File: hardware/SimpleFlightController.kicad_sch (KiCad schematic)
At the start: 0 parts

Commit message: Battery Charger 80% Done
I ended up finishing wiring all the pins except for the battery related ones, I'll finish those tomorrow and I'll move on to the sensors.
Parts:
- added C2: 44uF, symbol Device:C
- added C3, C4, C6: 10uF, symbol Device:C
- added C5: 1uf, symbol Device:C
- added C7: 47uF, symbol Device:C
- added CARD1: DM3C-SF, easyeda2kicad:TF-SMD_DM3CS-SF, symbol LSCS_Parts:DM3C-SF
- added D1: LED, symbol Device:LED
- added J1: Screw_Terminal_01x02, symbol Connector:Screw_Terminal_01x02
- added L1: 1μH, symbol Device:L
- added R1, R2: 5.1K, symbol Device:R
- added R10: 5.23k, symbol Device:R
- added R11: 383, symbol Device:R
- added R14, R4, R5, R6: 10k, symbol Device:R
- added R3: 2.2k, symbol Device:R
- added R8: 10K, symbol Device:R
- added R9: 30.1k, symbol Device:R
- added U1: TPS63070RNMR, easyeda2kicad:VQFN-15_L3.0-W2.5-P0.50-BL, symbol LSCS_Parts:TPS63070RNMR
- added U2: ABX00027, easyeda2kicad:COMM-SMD_ABX00027, symbol LSCS_Parts:ABX00027
- added U3: ICM-20948, easyeda2kicad:QFN-24_L3.0-W3.0-P0.40-BL-EP, symbol LSCS_Parts:ICM-20948
- added U4: BME280, easyeda2kicad:LGA-8_BME280_BL, symbol LSCS_Parts:BME280
- added U5: BQ25887RGET, easyeda2kicad:VQFN-24_L4.0-W4.0-P0.50-TL-EP2.7, symbol LSCS_Parts:BQ25887RGET
- added U6: LMR51430XDDCR, easyeda2kicad:SOT-23-6_L2.9-W1.6-P0.95-LS2.8-BL, symbol LSCS_Parts:LMR51430XDDCR
- added USB1: TYPE-C 16PIN 2MD, easyeda2kicad:USB-C-SMD_TYPE-C-16PIN-2MD-073, symbol LSCS_Parts:TYPE-C16PIN2MD
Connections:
- new net: D1.1 (K), U5.2 (STAT)
- new net: D1.2 (A), R3.2
- new net: R2.1, USB1.B5 (CC2)
- new net: C4.1, C6.2, L1.1, U5.21 (PMID), U5.22 (PMID)
- new net: C2.1, U5.15 (SNS), U5.16 (SNS)
- new net: C7.1, U5.12 (BTST)
- new net: R14.1, U5.7 (TS)
- new net: R11.1, U5.8 (ILIM)
- new net: R10.1, R9.2
- new net: R1.1, USB1.A5 (CC1)
- new net +3.3V: R3.1, R4.1, R5.1, R6.1, R8.2
- new net +3V3: R10.2
- new net +BAT: C3.1, J1.1 (Pin_1), U5.13 (BAT), U5.14 (BAT)
- new net BQ_CD: U5.3 (CD)
- new net BQ_INT: R6.2, U5.6 (~{INT})
- new net BQ_PG: R8.1, U5.1 (~{PG})
- new net BQ_PSEL: U5.24 (PSEL)
- new net BTST: C7.2, L1.2, U5.17 (SW), U5.18 (SW)
- new net GND: C2.2, C3.2, C4.2, C5.2, C6.1, J1.2 (Pin_2), R1.2, R11.2, R14.2, R2.2, R9.1, U5.11 (REGN), U5.19 (GND), U5.20 (GND), U5.25 (EP), USB1.13 (EH), USB1.14 (EH), USB1.A1B12 (GND), USB1.B1A12 (GND)
- new net I2C_SCL: R5.2, U5.5 (SCL)
- new net I2C_SDA: R4.2, U5.4 (SDA)
- new net USB_DN: USB1.A7 (Dn1), USB1.B7 (Dn2)
- new net USB_DP: USB1.A6 (Dp1), USB1.B6 (Dp2)
- new net VBUS: C5.1, U5.23 (VBUS), USB1.A4B9 (VBUS), USB1.B4A9 (VBUS)
- no-connect marks 0 -> 2

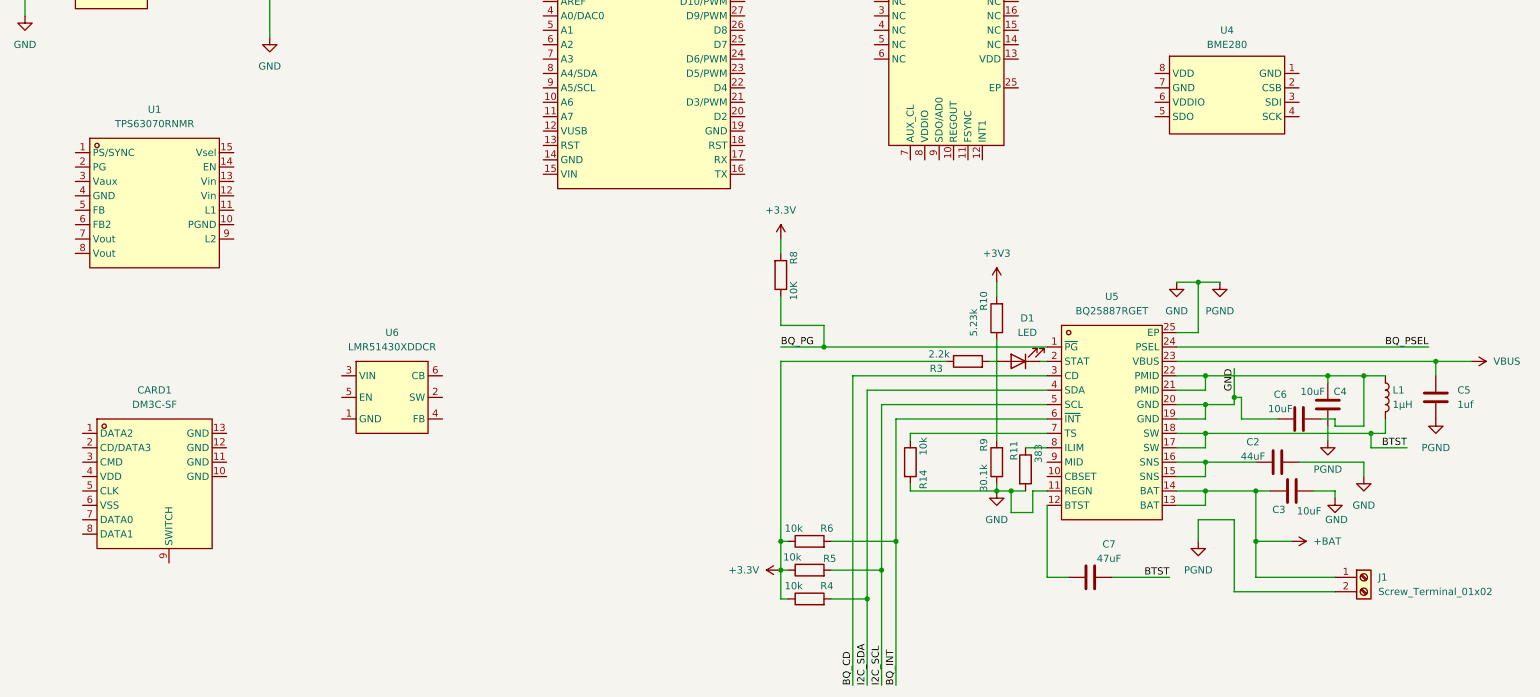
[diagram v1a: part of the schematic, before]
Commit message: 5/22/2026: Finished Regulator, Sensor, and Tracker
Everything went smoothly, using the datasheets for so long has given me a better understanding on what each symbol means/does.
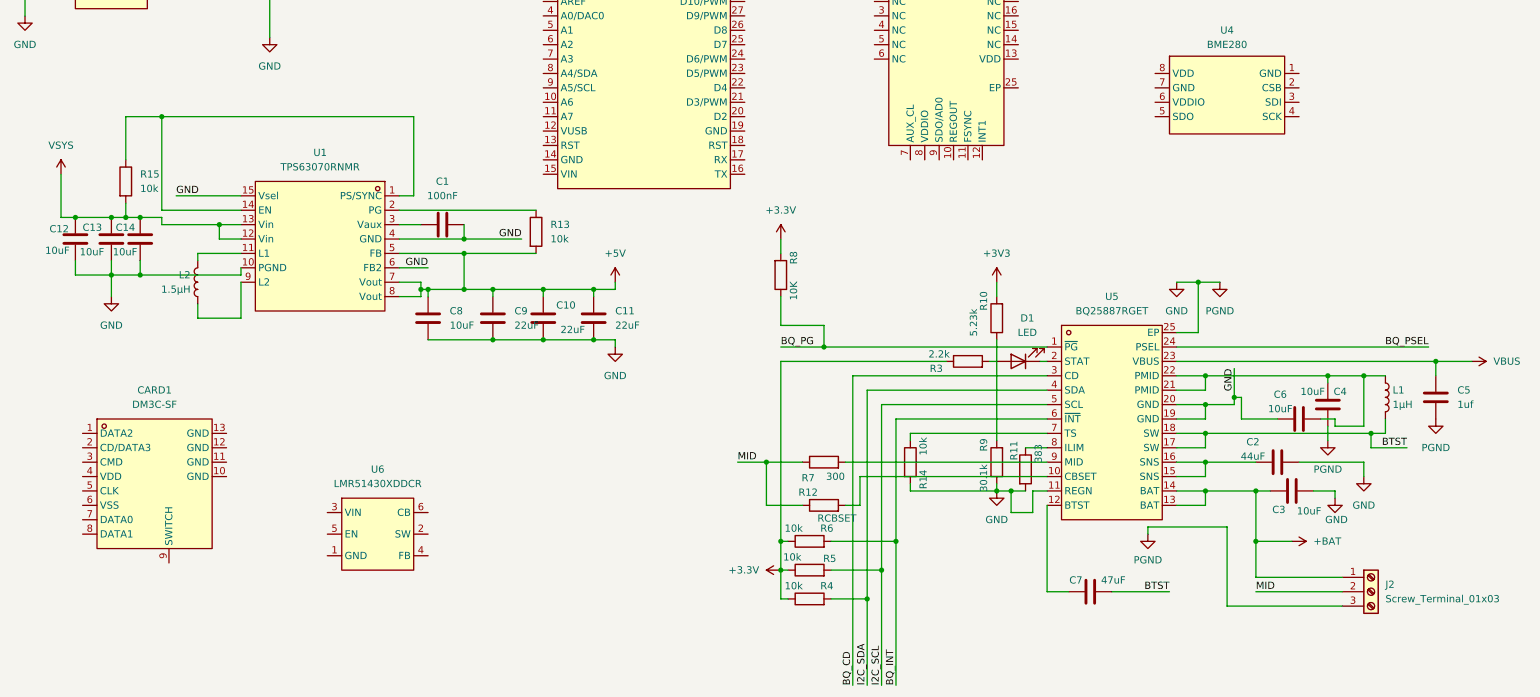
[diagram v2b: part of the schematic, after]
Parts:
- removed J1: Screw_Terminal_01x02, symbol Connector:Screw_Terminal_01x02
- added C1: 100nF, symbol Device:C
- added C10, C11, C9: 22uF, symbol Device:C
- added C12, C13, C14, C8: 10uF, symbol Device:C
- added J2: Screw_Terminal_01x03, symbol Connector:Screw_Terminal_01x03
- added L2: 1.5μH, symbol Device:L
- added R12: RCBSET, symbol Device:R
- added R13, R15: 10k, symbol Device:R
- added R7: 300, symbol Device:R
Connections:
- net +BAT: now also J2.1 (Pin_1)
- net GND: now also U1.10 (PGND), U1.15 (Vsel), U1.4 (GND), U1.6 (FB2), C1.1, C10.2, C11.2, C12.2, C13.2, C14.2, C8.2, C9.2, J2.3 (Pin_3)
- net at U5.10 (CBSET): now also R12.2
- net at U5.9 (MID): now also R7.2
- net at U1.1 (PS/SYNC): now also U1.14 (EN), R15.1
- net at U1.11 (L1): now also L2.1
- net VSYS: now reaches U1.12 (Vin)
- net VSYS: now also U1.13 (Vin), C12.1, C13.1, C14.1, R15.2
- net at U1.2 (PG): now also R13.1
- net at U1.3 (Vaux): now also C1.2
- net +5V: now reaches U1.5 (FB)
- net +5V: now also U1.7 (Vout), U1.8 (Vout), C10.1, C11.1, C8.1, C9.1, R13.2
- net at U1.9 (L2): now also L2.2
- new net MID: J2.2 (Pin_2), R12.1, R7.1
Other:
- moved on the sheet: C7, U1, U6

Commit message: Finished Schematic
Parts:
- removed U2: ABX00027, easyeda2kicad:COMM-SMD_ABX00027, symbol LSCS_Parts:ABX00027
- added C15: 2.2μF, symbol Device:C
- added C16, C17: 22μF, symbol Device:C
- added C18, C19, C20, C26, C27, C28, C29, C30, C39: 100nF, symbol Device:C
- added C21: C, symbol Device:C
- added C22, C24: 100uF, symbol Device:C
- added C25: 2.2uF, symbol Device:C
- added C31, C32, C33, C34: 1uF, symbol Device:C
- added C35, C36: 6.8pF, symbol Device:C
- added C37, C38: 20pF, symbol Device:C
- added J1, J3: Conn_01x03, symbol Connector_Generic:Conn_01x03
- added L3: 5.6μH, symbol Device:L
- added L4: FCM1608KF-601T03, easyeda2kicad:L0603, symbol LSCS_Parts:FCM1608KF-601T03
- added R16: 22.1k, symbol Device:R
- added R17: 100k, symbol Device:R
- added R18, R19, R20, R21, R22, R23, R24: 10k, symbol Device:R
- added SW1, SW2: TS-1088-AR02016, easyeda2kicad:SW-SMD_L3.9-W3.0-P4.45, symbol LSCS_Parts:TS-1088-AR02016
- added U7: STM32F722RETx, Package_QFP:LQFP-64_10x10mm_P0.5mm, symbol MCU_ST_STM32F7:STM32F722RETx
- added X1: X322525MOB4SI, easyeda2kicad:CRYSTAL-SMD_4P-L3.2-W2.5-BL, symbol LSCS_Parts:X322525MOB4SI
- added X2: Q13FC1350000400, easyeda2kicad:FC-135R_L3.2-W1.5, symbol LSCS_Parts:Q13FC1350000400
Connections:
- net +3.3V: now also CARD1.4 (VDD), U3.13 (VDD), U3.8 (VDDIO), U4.2 (CSB), U4.6 (VDDIO), U4.8 (VDD), C16.1, C17.1, C19.1, C20.1, C21.2, C24.1, C26.1, C27.1, C28.1, C29.1, C30.1, C31.1, C32.1, C33.1, C34.1, L3.2, L4.1, R18.1, R19.1, R20.1, R21.1, R22.1, R23.1, SW2.1, U7.1 (VBAT), U7.19 (VDD), U7.32 (VDD), U7.48 (VDD), U7.64 (VDD)
- net +5V: now also J1.1 (Pin_1), J3.1 (Pin_1)
- net BQ_INT: now also U7.57 (PB5)
- net GND: now also CARD1.10 (GND), CARD1.11 (GND), CARD1.12 (GND), CARD1.13 (GND), CARD1.6 (VSS), U3.18 (GND), U4.1 (GND), U4.5 (SDO), U4.7 (GND), U6.1 (GND), C15.2, C16.2, C17.2, C19.2, C20.2, C21.1, C22.2, C24.2, C25.2, C26.2, C27.2, C28.2, C29.2, C30.2, C31.2, C32.2, C33.2, C34.2, C35.2, C36.2, C37.2, C38.2, C39.1, J1.3 (Pin_3), J3.3 (Pin_3), R16.2, R24.2, SW1.1, U7.12 (VSSA), U7.18 (VSS), U7.31 (VSS), U7.47 (VSS), U7.63 (VSS), X1.2 (GND), X1.4 (GND)
- net I2C_SCL: now also U4.4 (SCK), U7.58 (PB6)
- net I2C_SDA: now also U4.3 (SDI), U7.59 (PB7)
- net USB_DN: now also U7.44 (PA11)
- net USB_DP: now also U7.45 (PA12)
- net VSYS: now also U6.3 (VIN), U6.5 (EN), C15.1
- net at D1.2 (A), R3.2: now also R10.1
- net SD_DAT2: now reaches CARD1.1 (DATA2)
- net SD_DAT2: now also R23.2, U7.51 (PC10)
- net SD_DAT3: now reaches CARD1.2 (CD/DATA3)
- net SD_DAT3: now also R22.2, U7.52 (PC11)
- net SD_CMD: now reaches CARD1.3 (CMD)
- net SD_CMD: now also R21.2, U7.54 (PD2)
- net SD_CLK: now reaches CARD1.5 (CLK)
- net SD_CLK: now also R20.2, U7.53 (PC12)
- net SD_DAT0: now reaches CARD1.7 (DATA0)
- net SD_DAT0: now also R19.2, U7.39 (PC8)
- net SD_DAT1: now reaches CARD1.8 (DATA1)
- net SD_DAT1: now also R18.2, U7.40 (PC9)
- net at U6.2 (SW): now also C18.2, L3.1, R17.1
- net at U6.4 (FB): now also R16.1, R17.2
- net at U6.6 (CB): now also C18.1
- net at U3.10 (REGOUT): now also C22.1
- net ICM_FSYNC: now reaches U3.11 (FSYNC)
- net ICM_INT1: now reaches U3.12 (INT1)
- net ICM_INT1: now also U7.24 (PC4), U7.41 (PA8)
- net ICM_nCS: now reaches U3.22 (nCS)
- net ICM_SCL: now reaches U3.23 (SCL/SCLK)
- net ICM_SDI: now reaches U3.24 (SDA/SDI)
- net ICM_SDI: now also U7.23 (PA7)
- net ICM_SDO: now reaches U3.9 (SDO/AD0)
- net ICM_SDO: now also U7.22 (PA6)
- net at R9.2: no longer R10.1
- new net: L4.2, U7.13 (VDDA)
- new net: C25.1, U7.30 (VCAP_1)
- new net BMP_INT: U7.62 (PB9)
- new net BOOT: R24.1, SW2.2, U7.60 (BOOT0)
- new net BQ_CE: U7.61 (PB8)
- new net HSE_IN: C38.1, U7.5 (PH0), X1.1 (OSC1)
- new net HSE_OUT: C37.1, U7.6 (PH1), X1.3 (OSC2)
- new net ICM_CS: U7.20 (PA4)
- new net ICM_INT2: U7.25 (PB0), U7.42 (PA9)
- new net ICM_SCK: U7.21 (PA5)
- new net LSE_IN: C36.1, U7.3 (PC14), X2.1
- new net LSE_OUT: C35.1, U7.4 (PC15), X2.2
- new net RESET: C39.2, SW1.2, U7.7 (NRST)
- new net SD_CD: U7.55 (PB3)
- new net SERVO1: J1.2 (Pin_2), U7.14 (PA0)
- new net SERVO2: J3.2 (Pin_2), U7.15 (PA1)
- no-connect marks 2 -> 39
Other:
- title: (none) -> Simple Flight Controller
- moved on the sheet: C1, C10, C11, C12, C13, C14, C2, C3, C4, C5, C6, C7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

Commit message: PCB Footprints
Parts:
- C1, C12, C13, C14, C15, C18, C19, C20, C22, C24, C25, C26, C27, C28, C29, C3, C30, C31, C32, C33, C34, C35, C36, C37, C38, C39, C4, C5, C6, C8: footprint (none) -> Capacitor_SMD:C_0402_1005Metric
- C10, C11, C16, C17, C2, C7, C9: footprint (none) -> Capacitor_SMD:C_0805_2012Metric
- C21: value C -> 100nF; footprint (none) -> Capacitor_SMD:C_0402_1005Metric
- D1: footprint (none) -> LED_SMD:LED_0402_1005Metric
- J1, J3: footprint (none) -> Connector_PinHeader_2.54mm:PinHeader_2x03_P2.54mm_Vertical
- J2: footprint (none) -> TerminalBlock:TerminalBlock_Xinya_XY308-2.54-3P_1x03_P2.54mm_Horizontal
- L1: footprint (none) -> Inductor_SMD:L_1008_2520Metric
- L2: footprint (none) -> Inductor_SMD:L_APV_ANR4012
- L3: footprint (none) -> Inductor_SMD:L_1210_3225Metric
- R1, R10, R11, R12, R13, R14, R15, R16, R17, R18, R19, R2, R20, R21, R22, R23, R24, R3, R4, R5, R6, R7, R8, R9: footprint (none) -> Resistor_SMD:R_0201_0603Metric

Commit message: PCB Routing
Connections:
- net +5V: no longer U1.8 (Vout)
- net VSYS: no longer U1.13 (Vin)
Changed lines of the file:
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@@
 		(pin "7"
 		)
-		(pin "8"
+		(pin "7"
 		)
 		(pin "10"
@@
 		(pin "12"
 		)
-		(pin "13"
+		(pin "12"
 		)
 		(pin "15"
